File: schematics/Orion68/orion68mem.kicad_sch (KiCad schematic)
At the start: 14 parts, among them J100 Euro96pin, J7 JMP_PIN3, J8 JMP_PIN31, J9 JMP_PIN29, U100 GAL20V8, U101 RAM_LOW, U102 RAM_HIGH, U103 RAM_LOW, U104 RAM_HIGH, U105 RAM_LOW, U106 RAM_HIGH, U107 RAM_LOW, U108 RAM_HIGH

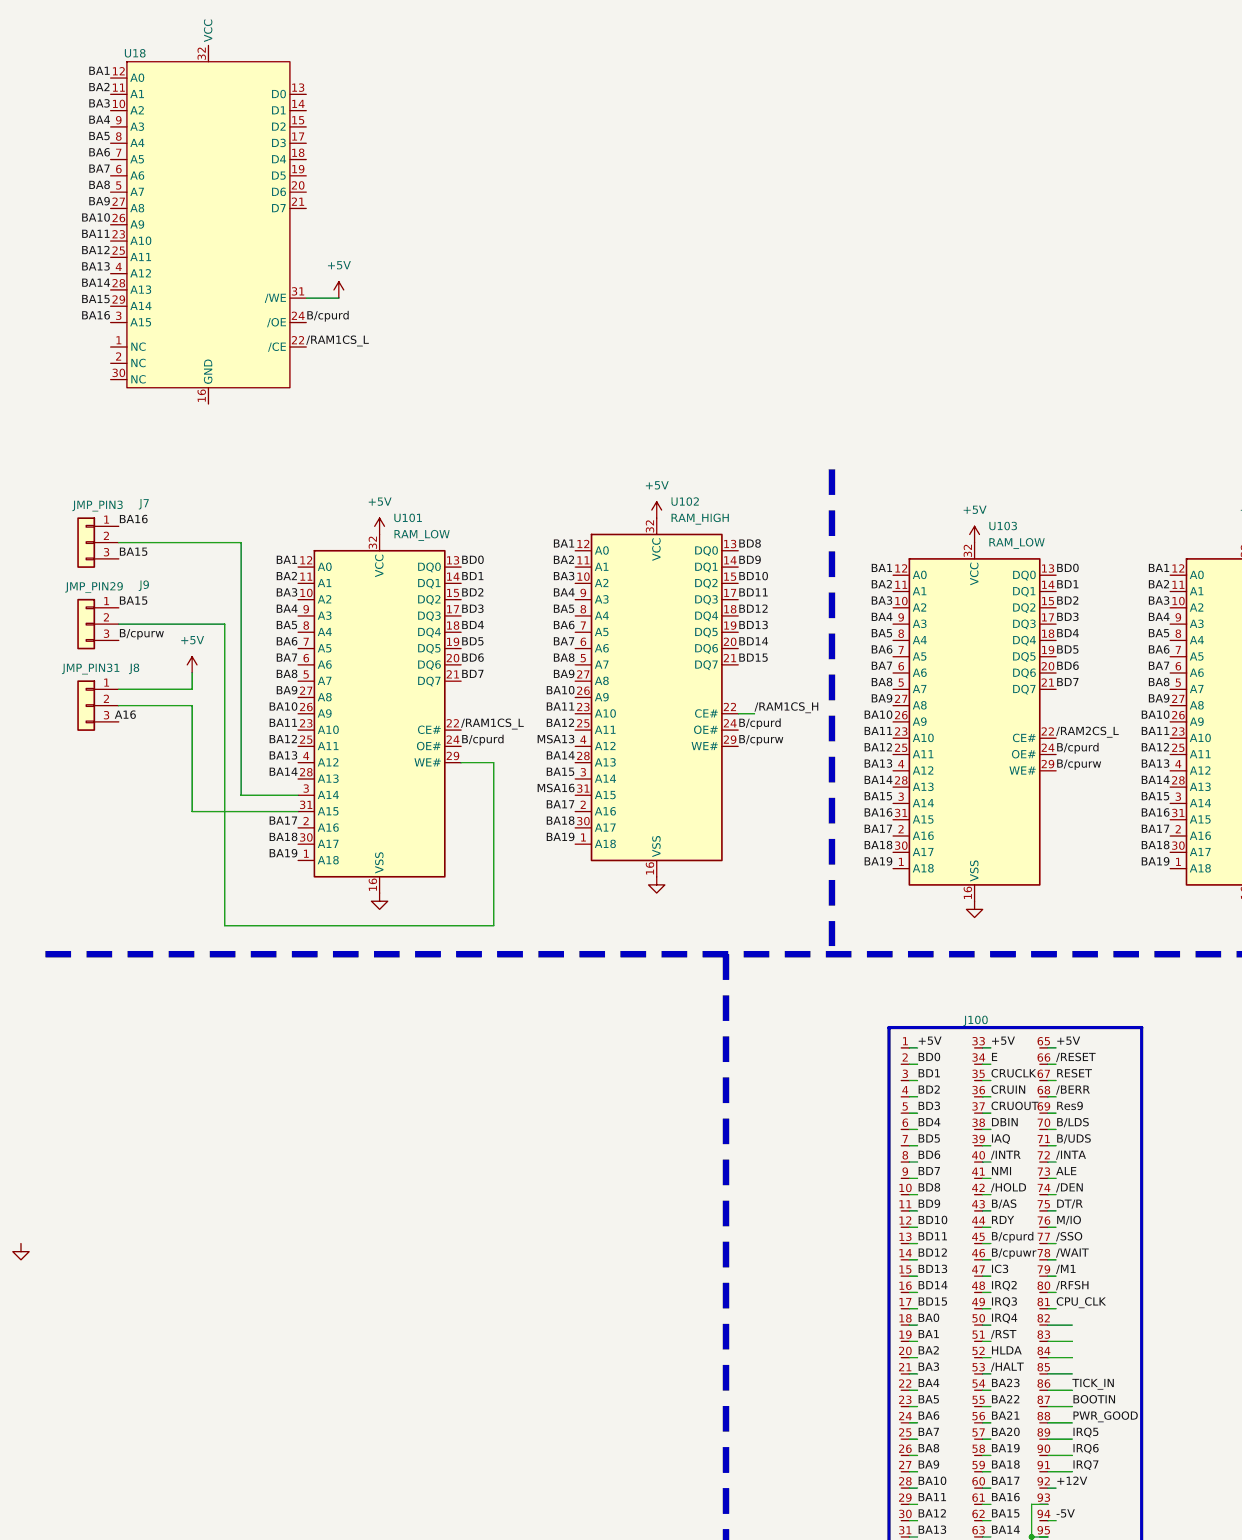
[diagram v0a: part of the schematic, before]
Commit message: A20 bug fixed, missing serial CSA, running ok
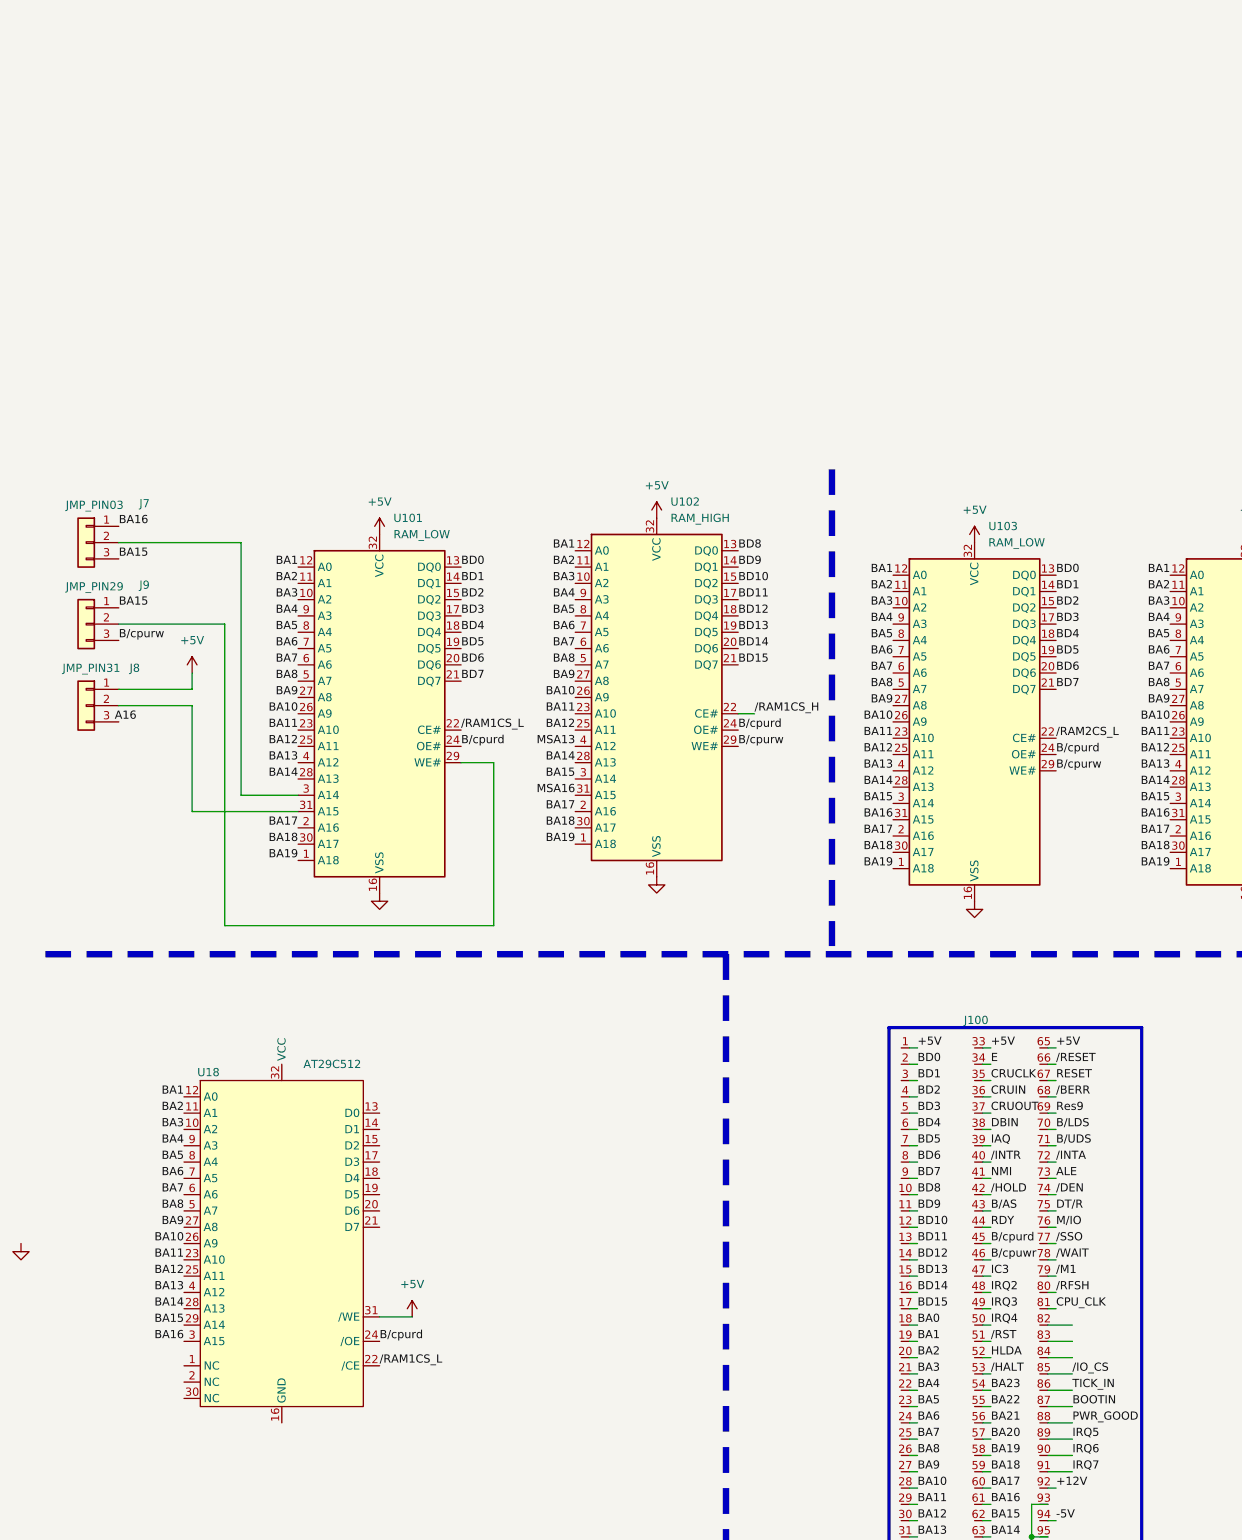
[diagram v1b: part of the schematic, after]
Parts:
- J7: value JMP_PIN3 -> JMP_PIN03
- U18: value ~ -> AT29C512
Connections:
- net /IO_CS: now reaches J100.85
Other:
- moved on the sheet: U18
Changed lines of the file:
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@@
 	(wire
 		(pts
-			(xy 58.42 -15.24) (xy 53.34 -15.24)
+			(xy 69.85 143.51) (xy 64.77 143.51)
 		)
 		(stroke
@@
 		)
 	)
+	(label "{slash}IO_CS"
+		(at 172.72 152.4 0)
+		(effects
+			(font
+				(size 1.27 1.27)
+			)
+			(justify left bottom)
+		)
+	)
 	(label "BA19"
 		(at 187.96 73.66 180)
@@
 	)
 	(label "BA8"
-		(at 22.86 -31.75 180)
+		(at 34.29 127 180)
 		(effects
 			(font
@@
 	)
 	(label "BA5"
-		(at 22.86 -39.37 180)
+		(at 34.29 119.38 180)
 		(effects
 			(font
@@
 	)
 	(label "BA10"
-		(at 22.86 -26.67 180)
+		(at 34.29 132.08 180)
 		(effects
 			(font
@@
 	)
 	(label "BA12"
-		(at 22.86 -21.59 180)
+		(at 34.29 137.16 180)
 		(effects
 			(font
@@
 	)
 	(label "BA6"
-		(at 22.86 -36.83 180)
+		(at 34.29 121.92 180)
 		(effects
 			(font
@@
 	)
 	(label "BA3"
-		(at 22.86 -44.45 180)
+		(at 34.29 114.3 180)
 		(effects
 			(font
@@
 	)
 	(label "{slash}RAM1CS_L"
-		(at 53.34 -7.62 0)
+		(at 64.77 151.13 0)
 		(effects
 			(font
@@
 	)
 	(label "BA9"
-		(at 22.86 -29.21 180)
+		(at 34.29 129.54 180)
 		(effects
 			(font
@@
 	)
 	(label "B{slash}cpurd"
-		(at 53.34 -11.43 0)
+		(at 64.77 147.32 0)
 		(effects
 			(font
@@
 	)
 	(label "BA14"
-		(at 22.86 -16.51 180)
+		(at 34.29 142.24 180)
 		(effects
 			(font
@@
 	)
 	(label "BA13"
-		(at 22.86 -19.05 180)
+		(at 34.29 139.7 180)
 		(effects
 			(font
@@
 	)
 	(label "BA11"
-		(at 22.86 -24.13 180)
+		(at 34.29 134.62 180)
 		(effects
 			(font
@@
 	)
 	(label "BA2"
-		(at 22.86 -46.99 180)
+		(at 34.29 111.76 180)
 		(effects
 			(font
@@
 	)
 	(label "BA15"
-		(at 22.86 -13.97 180)
+		(at 34.29 144.78 180)
 		(effects
 			(font
@@
 	)
 	(label "BA7"
-		(at 22.86 -34.29 180)
+		(at 34.29 124.46 180)
 		(effects
 			(font
@@
 	)
 	(label "BA4"
-		(at 22.86 -41.91 180)
+		(at 34.29 116.84 180)
 		(effects
 			(font
@@
 	)
 	(label "BA16"
-		(at 22.86 -11.43 180)
+		(at 34.29 147.32 180)
 		(effects
 			(font
@@
 	)
 	(label "BA1"
-		(at 22.86 -49.53 180)
+		(at 34.29 109.22 180)
 		(effects
 			(font
@@
 	(symbol
 		(lib_id "power:+5V")
-		(at 58.42 -15.24 0)
+		(at 69.85 143.51 0)
 		(unit 1)
 		(exclude_from_sim no)
@@
 		(fields_autoplaced yes)
 		(property "Reference" "#PWR0124"
-			(at 58.42 -11.43 0)
+			(at 69.85 147.32 0)
 			(effects
 				(font
@@
 		)
 		(property "Value" "+5V"
-			(at 58.42 -20.32 0)
+			(at 69.85 138.43 0)
 			(effects
 				(font
@@
 		)
 		(property "Footprint" ""
-			(at 58.42 -15.24 0)
+			(at 69.85 143.51 0)
 			(effects
 				(font
@@
 		)
 		(property "Datasheet" ""
-			(at 58.42 -15.24 0)
+			(at 69.85 143.51 0)
 			(effects
 				(font
@@
 		)
 		(property "Description" "Power symbol creates a global label with name \"+5V\""
-			(at 58.42 -15.24 0)
+			(at 69.85 143.51 0)
 			(effects
 				(font
@@
 			)
 		)
-		(property "Value" "JMP_PIN3"
+		(property "Value" "JMP_PIN03"
 			(at 24.892 17.018 0)
 			(effects
@@
 	(symbol
 		(lib_id "pdSilva:AT29C512")
-		(at 38.1 -53.34 0)
+		(at 49.53 105.41 0)
 		(unit 1)
 		(exclude_from_sim no)
@@
 		(on_board yes)
 		(dnp no)
-		(fields_autoplaced yes)
 		(property "Reference" "U18"
-			(at 26.67 -53.34 0)
+			(at 38.1 105.41 0)
 			(do_not_autoplace yes)
 			(effects
@@
 			)
 		)
-		(property "Value" "~"
-			(at 38.1 -55.88 0)
+		(property "Value" "AT29C512"
+			(at 57.404 104.14 0)
 			(effects
 				(font
@@
 		)
 		(property "Footprint" ""
-			(at 38.1 -53.34 0)
+			(at 49.53 105.41 0)
 			(effects
 				(font
@@
 		)
 		(property "Datasheet" ""
-			(at 38.1 -53.34 0)
+			(at 49.53 105.41 0)
 			(effects
 				(font
@@
 		)
 		(property "Description" ""
-			(at 38.1 -53.34 0)
+			(at 49.53 105.41 0)
 			(effects
 				(font

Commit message: updating
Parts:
- added U25, U26: 74HC138, symbol 74xx:74HC138
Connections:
- net +5V: now also U25.16 (VCC), U25.6 (E2), U26.16 (VCC), U26.6 (E2)
- net GND: now also U25.3 (A2), U25.8 (GND), U26.3 (A2), U26.8 (GND)
- net /IO_CS: now also J100.84; no longer J100.85
- net /UART_CS: now reaches J100.83
- new net A19: U25.1 (A0), U26.1 (A0)
- new net A20: U25.2 (A1), U26.2 (A1)
- new net RAM1_H: U26.14 (~{Y1})
- new net RAM1_L: U25.14 (~{Y1})
- new net RAM2_H: U26.13 (~{Y2})
- new net RAM2_L: U25.13 (~{Y2})
- new net RAM3_H: U26.12 (~{Y3})
- new net RAM3_L: U25.12 (~{Y3})
- new net ROM_H: U26.15 (~{Y0})
- new net ROM_L: U25.15 (~{Y0})
- new net /LDS: U25.5 (~{E1})
- new net /MEM_CS: J100.85, U25.4 (~{E0})
- new net /UDS: U26.5 (~{E1})
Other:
- moved on the sheet: U100

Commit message: B column DIN conn. all in GND
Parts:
- removed J100: Euro96pin, ConnPdSilva:conn_euro96, symbol ConnPdSilva:ConnEuro96
- added J100 (x2): Euro96pin, ConnPdSilva:conn_euro96, symbol ConnPdSilva:ConnEuro96
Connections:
- net +12V: now also J100.92, J100.92
- net +5V: now also J100.1, J100.1, J100.33, J100.33, J100.65, J100.65
- net -5V: now also J100.94, J100.94
- net A16: now also J8.3 (Pin_3)
- net ALE: now also J100.73
- net BA0: now also J100.18
- net BA1: now also J100.19, J100.19
- net BA10: now also J100.28, J100.28
- net BA11: now also J100.29, J100.29
- net BA12: now also J100.30, J100.30
- net BA13: now also J100.31, J100.31
- net BA14: now also J100.63, J100.91
- net BA15: now also J100.62, J100.90
- net BA16: now also J100.61, J100.89
- net BA17: now also J100.60, J100.88
- net BA18: now also J100.59, J100.87
- net BA19: now also J100.58, J100.86
- net BA2: now also J100.20, J100.20
- net BA20: now also J100.57, J100.81
- net BA21: now also J100.56, J100.80
- net BA22: now also J100.55, J100.79
- net BA23: now also J100.54, J100.78
- net BA3: now also J100.21, J100.21
- net BA4: now also J100.22, J100.22
- net BA5: now also J100.23, J100.23
- net BA6: now also J100.24, J100.24
- net BA7: now also J100.25, J100.25
- net BA8: now also J100.26, J100.26
- net BA9: now also J100.27, J100.27
- net BD0: now also J100.2, J100.2
- net BD1: now also J100.3, J100.3
- net BD10: now also J100.12, J100.12
- net BD11: now also J100.13, J100.13
- net BD12: now also J100.14, J100.14
- net BD13: now also J100.15, J100.15
- net BD14: now also J100.16, J100.16
- net BD15: now also J100.17, J100.17
- net BD2: now also J100.4, J100.4
- net BD3: now also J100.5, J100.5
- net BD4: now also J100.6, J100.6
- net BD5: now also J100.7, J100.7
- net BD6: now also J100.8, J100.8
- net BD7: now also J100.9, J100.9
- net BD8: now also J100.10, J100.10
- net BD9: now also J100.11, J100.11
- net BOOTIN: now also J100.87
- net B/AS: now also J100.43, J100.69
- net B/LDS: now also J100.70, J100.70
- net B/UDS: now also J100.71, J100.71
- net CPU_CLK: now also J100.81
- net CRUCLK: now also J100.35
- net CRUIN: now also J100.36
- net CRUOUT: now also J100.37
- net DBIN: now also J100.38
- net DT/R: now also J100.75
- net E: now also J100.34
- net GND: now also J100.32, J100.32, J100.64, J100.64, J100.93, J100.93, J100.95, J100.95, J100.96, J100.96
- net HLDA: now also J100.52
- net IAQ: now also J100.39
- net IRQ2: now also J100.48
- net IRQ3: now also J100.49
- net IRQ4: now also J100.50
- net IRQ5: now also J100.89
- net IRQ6: now also J100.90
- net IRQ7: now also J100.91
- net M/IO: now also J100.76
- net NMI: now also J100.41
- net PWR_GOOD: now also J100.88
- net RESET: now also J100.67, J100.67
- net Res9: now also J100.69
- net TICK_IN: now also J100.86
- net /BERR: now also J100.68
- net /DEN: now also J100.74
- net /HALT: now also J100.53
- net /HOLD: now also J100.42
- net /INTA: now also J100.72
- net /INTR: now also J100.40
- net /IO_CS: now also J100.84, J100.84
- net /M1: now also J100.79
- net /MEM_CS: now also J100.85, J100.85
- net /RESET: now also J100.66, J100.66
- net /RFSH: now also J100.80
- net /RST: now also J100.51
- net /SSO: now also J100.77
- net /UART_CS: now also J100.83
- net /WAIT: now also J100.78
- new net /IO_CS1: J100.82, J100.82
- new net /iord: J100.44
- new net /iowr: J100.47
- new net /memrd: J100.45
- new net /memwr: J100.46
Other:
- note added: "1 2 3 4 5 6 7 8 9 10 11 12 13 14 15"
- note added: "15 14 13 12 11 10"
- note added: "15 14 13 12 11 10 9 8 7 6 5 4 3 2 1"
- moved on the sheet: U100

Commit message: Update vbug2.0
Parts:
- added U23: ~, symbol pdSilva:74HC4078
- added U27: 74LS32, symbol 74xx:74LS32
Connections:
- net A19: now also U23.4 (I3)
- net A20: now also U23.5 (I4)
- net /memrd: now also U27.4
- net /memwr: now also U27.2
- new net: U23.1 (O1), U27.1, U27.5
- new net A17: U23.2 (I1)
- new net A18: U23.3 (I2)
- new net A21: U23.9 (I5)
- new net A22: U23.10 (I6)
- new net A23: U23.11 (I7)
- new net /ram: U27.3
- new net /rom: U27.6
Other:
- moved on the sheet: J100, U100, U105, U106, U107, U108

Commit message: Version 1.2 picoVGA implemented a workaround for the UART issue
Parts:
- removed J100 (x2): Euro96pin, ConnPdSilva:conn_euro96, symbol ConnPdSilva:ConnEuro96
- removed U100: GAL20V8, Package_DIP:DIP-24_W7.62mm_Socket, symbol plds:GAL20V8
- removed U105, U107: RAM_LOW, Package_DIP:DIP-32_W15.24mm, symbol Memory_RAM:AS6C4008-55PCN
- removed U106, U108: RAM_HIGH, Package_DIP:DIP-32_W15.24mm, symbol Memory_RAM:AS6C4008-55PCN
- removed U23: ~, symbol pdSilva:74HC4078
- removed U27: 74LS32, symbol 74xx:74LS32
- added J100: Euro96pin, ConnPdSilva:conn_euro96, symbol ConnPdSilva:ConnEuro96
- added J101B: TI9900_8BITS, symbol Connector_Generic:Conn_02x08_Counter_Clockwise
- added J13, J16, J17, J18, J7: J100A, symbol Connector_Generic:Conn_01x03
- added J14, J8: J100B, symbol Connector_Generic:Conn_01x03
- added J15, J9: J100C, symbol Connector_Generic:Conn_01x03
- added J20: J101A, symbol Connector_Generic:Conn_01x03
- added J30: rom2Rom5_30, symbol Connector_Generic:Conn_01x03
- added U103A, U104A, U105A: RAM_LOW, Package_DIP:DIP-32_W15.24mm, symbol Memory_RAM:AS6C4008-55PCN
- added U103B, U104B, U105B: RAM_HIGH, Package_DIP:DIP-32_W15.24mm, symbol Memory_RAM:AS6C4008-55PCN
- added U23: CY62256-70PC, Package_DIP:DIP-28_W15.24mm, symbol Memory_RAM:CY62256-70PC
- added U29: 28C256, symbol Memory_EEPROM:28C256
- J29: renamed from J9; value JMP_PIN29 -> ramRom29
- J3: renamed from J7; value JMP_PIN03 -> ramRom3
- J31: renamed from J8; value JMP_PIN31 -> ramRom31
- renumbered U25 to U100A, U26 to U100B, U101 to U101A, U102 to U101B, U103 to U102A, U104 to U102B
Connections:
- net MSA13 is gone; now on net BA13: U101B.4 (A12)
- net MSA16 is gone; now on net PIN31: U101B.31 (A15)
- net +12V: now also J100.92
- net +5V: now also J31.3 (Pin_3), J100.1, J100.33, J100.65, J18.1 (Pin_1), J30.3 (Pin_3), U103A.32 (VCC), U103B.32 (VCC), U104A.32 (VCC), U104B.32 (VCC), U105A.32 (VCC), U105B.32 (VCC); no longer J31.1 (Pin_1), U100A.6 (E2), U100B.6 (E2), U18.31 (/WE)
- net -5V: now also J100.94
- net A16: now also J31.1 (Pin_1); no longer J31.3 (Pin_3)
- net A19: now also J13.3 (Pin_3), J7.3 (Pin_3); no longer U100A.1 (A0), U100B.1 (A0)
- net A20: now also J14.3 (Pin_3), J8.3 (Pin_3); no longer U100A.2 (A1), U100B.2 (A1)
- net A21: now also J15.3 (Pin_3), J9.3 (Pin_3)
- net BA1: now also J100.19, U103A.12 (A0), U103B.12 (A0), U104A.12 (A0), U104B.12 (A0), U105A.12 (A0), U105B.12 (A0); no longer U18.12 (A0)
- net BA10: now also J100.28, U103A.26 (A9), U103B.26 (A9), U104A.26 (A9), U104B.26 (A9), U105A.26 (A9), U105B.26 (A9); no longer U18.26 (A9)
- net BA11: now also J100.29, U103A.23 (A10), U103B.23 (A10), U104A.23 (A10), U104B.23 (A10), U105A.23 (A10), U105B.23 (A10); no longer U18.23 (A10)
- net BA12: now also J100.30, U103A.25 (A11), U103B.25 (A11), U104A.25 (A11), U104B.25 (A11), U105A.25 (A11), U105B.25 (A11); no longer U18.25 (A11)
- net BA13: now also J100.31, U103A.4 (A12), U103B.4 (A12), U104A.4 (A12), U104B.4 (A12), U105A.4 (A12), U105B.4 (A12); no longer U18.4 (A12)
- net BA14: now also J100.91, U103A.28 (A13), U103B.28 (A13), U104A.28 (A13), U104B.28 (A13), U105A.28 (A13), U105B.28 (A13); no longer U18.28 (A13)
- net BA15: now also J29.3 (Pin_3), J3.1 (Pin_1), J100.90, U103A.3 (A14), U103B.3 (A14), U104A.3 (A14), U104B.3 (A14), U105A.3 (A14), U105B.3 (A14); no longer J29.1 (Pin_1), J3.3 (Pin_3), U101B.3 (A14), U18.29 (A14)
- net BA16: now also J3.3 (Pin_3), J100.89, U103A.31 (A15), U103B.31 (A15), U104A.31 (A15), U104B.31 (A15), U105A.31 (A15), U105B.31 (A15); no longer J3.1 (Pin_1), U18.3 (A15)
- net BA17: now also J100.88, U103A.2 (A16), U103B.2 (A16), U104A.2 (A16), U104B.2 (A16), U105A.2 (A16), U105B.2 (A16)
- net BA18: now also J100.87, J30.1 (Pin_1), U103A.30 (A17), U103B.30 (A17), U104A.30 (A17), U104B.30 (A17), U105A.30 (A17), U105B.30 (A17); no longer U101A.30 (A17), U101B.30 (A17)
- net BA19: now also J100.86, U103A.1 (A18), U103B.1 (A18), U104A.1 (A18), U104B.1 (A18), U105A.1 (A18), U105B.1 (A18)
- net BA2: now also J100.20, U103A.11 (A1), U103B.11 (A1), U104A.11 (A1), U104B.11 (A1), U105A.11 (A1), U105B.11 (A1); no longer U18.11 (A1)
- net BA20: now also J100.81
- net BA21: now also J100.80
- net BA22: now also J100.79
- net BA23: now also J100.78
- net BA3: now also J100.21, U103A.10 (A2), U103B.10 (A2), U104A.10 (A2), U104B.10 (A2), U105A.10 (A2), U105B.10 (A2); no longer U18.10 (A2)
- net BA4: now also J100.22, U103A.9 (A3), U103B.9 (A3), U104A.9 (A3), U104B.9 (A3), U105A.9 (A3), U105B.9 (A3); no longer U18.9 (A3)
- net BA5: now also J100.23, U103A.8 (A4), U103B.8 (A4), U104A.8 (A4), U104B.8 (A4), U105A.8 (A4), U105B.8 (A4); no longer U18.8 (A4)
- net BA6: now also J100.24, U103A.7 (A5), U103B.7 (A5), U104A.7 (A5), U104B.7 (A5), U105A.7 (A5), U105B.7 (A5); no longer U18.7 (A5)
- net BA7: now also J100.25, U103A.6 (A6), U103B.6 (A6), U104A.6 (A6), U104B.6 (A6), U105A.6 (A6), U105B.6 (A6); no longer U18.6 (A6)
- net BA8: now also J100.26, U103A.5 (A7), U103B.5 (A7), U104A.5 (A7), U104B.5 (A7), U105A.5 (A7), U105B.5 (A7); no longer U18.5 (A7)
- net BA9: now also J100.27, U103A.27 (A8), U103B.27 (A8), U104A.27 (A8), U104B.27 (A8), U105A.27 (A8), U105B.27 (A8); no longer U18.27 (A8)
- net BD0: now also J100.2, U103A.13 (DQ0), U104A.13 (DQ0), U105A.13 (DQ0)
- net BD1: now also J100.3, U103A.14 (DQ1), U104A.14 (DQ1), U105A.14 (DQ1)
- net BD10: now also J100.12, J101B.3 (Pin_3), U103B.15 (DQ2), U104B.15 (DQ2), U105B.15 (DQ2)
- net BD11: now also J100.13, J101B.4 (Pin_4), U103B.17 (DQ3), U104B.17 (DQ3), U105B.17 (DQ3)
- net BD12: now also J100.14, J101B.5 (Pin_5), U103B.18 (DQ4), U104B.18 (DQ4), U105B.18 (DQ4)
- net BD13: now also J100.15, J101B.6 (Pin_6), U103B.19 (DQ5), U104B.19 (DQ5), U105B.19 (DQ5)
- net BD14: now also J100.16, J101B.7 (Pin_7), U103B.20 (DQ6), U104B.20 (DQ6), U105B.20 (DQ6)
- net BD15: now also J100.17, J101B.8 (Pin_8), U103B.21 (DQ7), U104B.21 (DQ7), U105B.21 (DQ7)
- net BD2: now also J100.4, U103A.15 (DQ2), U104A.15 (DQ2), U105A.15 (DQ2)
- net BD3: now also J100.5, U103A.17 (DQ3), U104A.17 (DQ3), U105A.17 (DQ3)
- net BD4: now also J100.6, U103A.18 (DQ4), U104A.18 (DQ4), U105A.18 (DQ4)
- net BD5: now also J100.7, U103A.19 (DQ5), U104A.19 (DQ5), U105A.19 (DQ5)
- net BD6: now also J100.8, U103A.20 (DQ6), U104A.20 (DQ6), U105A.20 (DQ6)
- net BD7: now also J100.9, U103A.21 (DQ7), U104A.21 (DQ7), U105A.21 (DQ7)
- net BD8: now also J100.10, J101B.1 (Pin_1), U103B.13 (DQ0), U104B.13 (DQ0), U105B.13 (DQ0)
- net BD9: now also J100.11, J101B.2 (Pin_2), U103B.14 (DQ1), U104B.14 (DQ1), U105B.14 (DQ1)
- net B/AS: now also J100.69
- net B/LDS: now also J100.70
- net B/UDS: now also J100.71
- net B/cpurd: now also U103A.24 (OE#), U103B.24 (OE#), U104A.24 (OE#), U104B.24 (OE#), U105A.24 (OE#), U105B.24 (OE#); no longer U18.24 (/OE)
- net B/cpurw: now also U103A.29 (WE#), U103B.29 (WE#), U104A.29 (WE#), U104B.29 (WE#), U105A.29 (WE#), U105B.29 (WE#); no longer J29.3 (Pin_3), U101B.29 (WE#)
- net GND: now also J100.32, J100.64, J100.93, J100.95, J100.96, J14.1 (Pin_1), J15.1 (Pin_1), J8.1 (Pin_1), J9.1 (Pin_1), U103A.16 (VSS), U103B.16 (VSS), U104A.16 (VSS), U104B.16 (VSS), U105A.16 (VSS), U105B.16 (VSS); no longer U100A.3 (A2), U100B.3 (A2)
- net IRQ6: now also J100.68
- net RESET: now also J100.67
- net /IO_CS: now also J100.84
- net /IO_CS1: now also J100.82
- net /MEM_CS: now also U100B.4 (~{E0}), J100.85
- net /RAM1CS_H: now also U102B.22 (CE#); no longer U101B.22 (CE#)
- net /RAM1CS_L: now also U102A.22 (CE#); no longer U101A.22 (CE#), U18.22 (/CE)
- net /RAM2CS_H: now also U103B.22 (CE#); no longer U102B.22 (CE#)
- net /RAM2CS_L: now also U103A.22 (CE#); no longer U102A.22 (CE#)
- net /RAM3CS_H: now also U104B.22 (CE#)
- net /RAM3CS_L: now also U104A.22 (CE#)
- net /RAM4CS_H: now also U105B.22 (CE#)
- net /RAM4CS_L: now also U105A.22 (CE#)
- net /RESET: now also J100.66
- net /iord: now also J100.72
- net /iowr: now also J100.75
- net /memrd: now also J100.73
- net /memwr: now also J100.74
- net PIN29: now reaches J29.2 (Pin_2), U101A.29 (WE#)
- net PIN29: now also U101B.29 (WE#)
- net PIN3: now reaches J3.2 (Pin_2), U101A.3 (A14)
- net PIN3: now also U101B.3 (A14)
- net PIN31: now reaches J31.2 (Pin_2), U101A.31 (A15)
- net RAM4CS_H: now reaches U100B.11 (~{Y4})
- net RAM4CS_L: now reaches U100A.11 (~{Y4})
- net RAM1_H renamed RAM1CS_H
- net RAM1_L renamed RAM1CS_L
- net RAM2_H renamed RAM2CS_H
- net RAM2_L renamed RAM2CS_L
- net RAM3_H renamed RAM3CS_H
- net RAM3_L renamed RAM3CS_L
- net ROM_H renamed /MEM1CS_H
- net /MEM1CS_H: now also J20.1 (Pin_1)
- net ROM_L renamed /MEM1CS_L
- net /MEM1CS_L: now also U101A.22 (CE#), J20.3 (Pin_3)
- new net: J14.2 (Pin_2), U100B.2 (A1)
- new net: J13.1 (Pin_1), J17.2 (Pin_2)
- new net: J13.2 (Pin_2), U100B.1 (A0)
- new net: J20.2 (Pin_2), U101B.22 (CE#)
- new net: J16.2 (Pin_2), J7.1 (Pin_1)
- new net: J7.2 (Pin_2), U100A.1 (A0)
- new net: J18.2 (Pin_2), U100A.6 (E2), U100B.6 (E2)
- new net: J15.2 (Pin_2), U100B.3 (A2)
- new net: J9.2 (Pin_2), U100A.3 (A2)
- new net: J8.2 (Pin_2), U100A.2 (A1)
- new net B/cpuwr: J29.1 (Pin_1)
- new net PIN30: J30.2 (Pin_2), U101A.30 (A17), U101B.30 (A17)
- new net ROMRAM9900_CS: J16.1 (Pin_1), J17.1 (Pin_1)
- new net /A22: J18.3 (Pin_3)
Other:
- note added: "5 blocos de 2 soquetes 1 e 2 de 32 pinos cada Bloco 1 ROM ou RAM para cpu de 16 bits.(rom 28C64 ou 28c256 ou 29c512). ROm no soquete 1 e RAM no soquete 2 para cpu de 8bits( ROM 28c64, RAM 512K )"
- note added: "J101A 1-2 68k 2-3 TI_8BITS"
- note added: "J29 1-2 RAMxROM256 2-3 ROM512"
- note added: "J3 1-2 RAMxROM256 2-3 ROM512"
- note added: "J30 1-2 RAM 2-3 ROM256 E ROM512"
- note added: "J31 1-2 RAM 2-3 ROM512"
- note added: "REVER TODOS OS NUMEROS DOS JUMPERS ESTÁ BAGUNÇADO DEVIDO A CÓPIAS"
- note removed: "15 14 13 12 11 10"
- moved on the sheet: J29, J3, J31, U100A, U100B, U101A, U101B, U102A, U102B, U18
